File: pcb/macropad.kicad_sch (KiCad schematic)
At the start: 23 parts, among them SW1 SW_Push, SW2 SW_Push, SW3 SW_Push, SW4 SW_Push, SW5 SW_Push, SW6 SW_Push, SW7 SW_Push, SW8 SW_Push, SW9 SW_Push, U1 PICO_RP2040

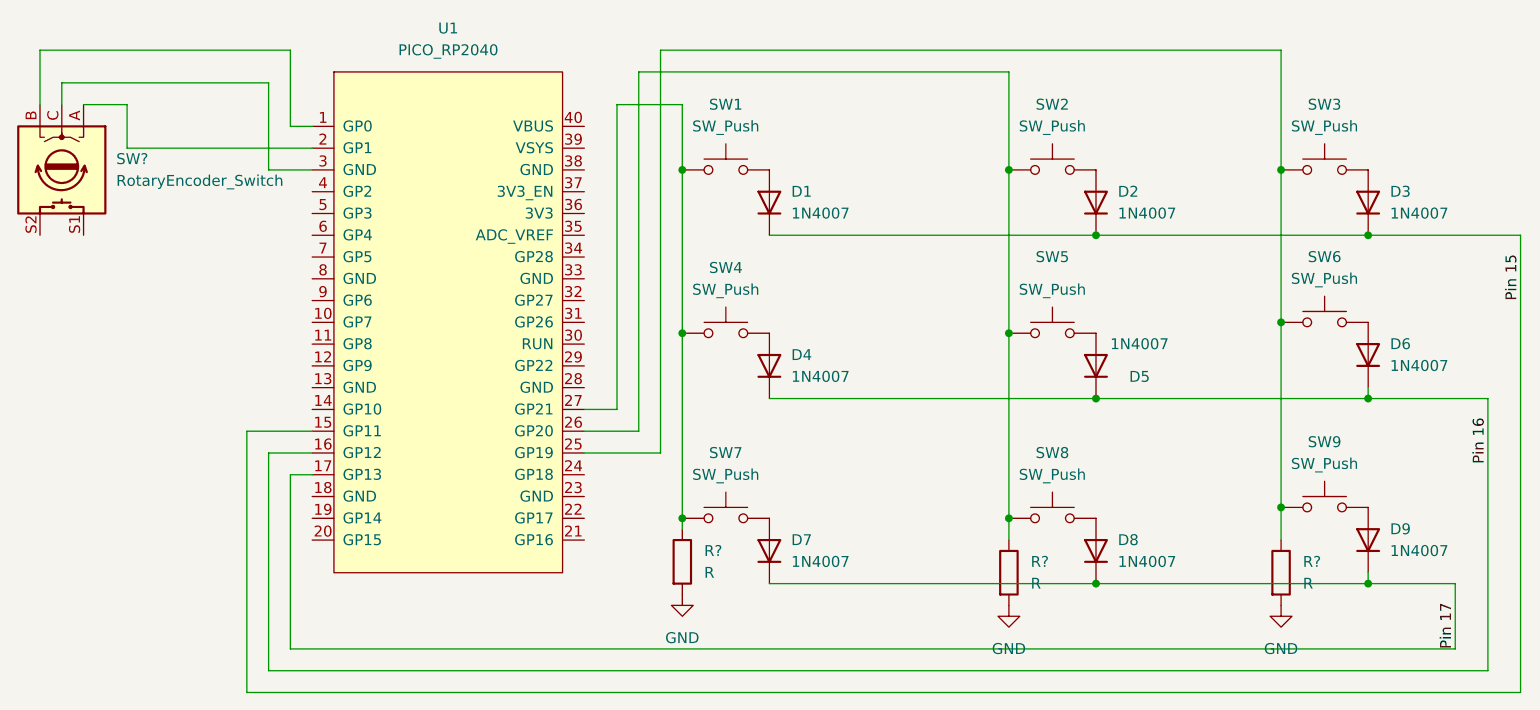
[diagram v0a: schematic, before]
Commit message: Corrected footprints for resistors
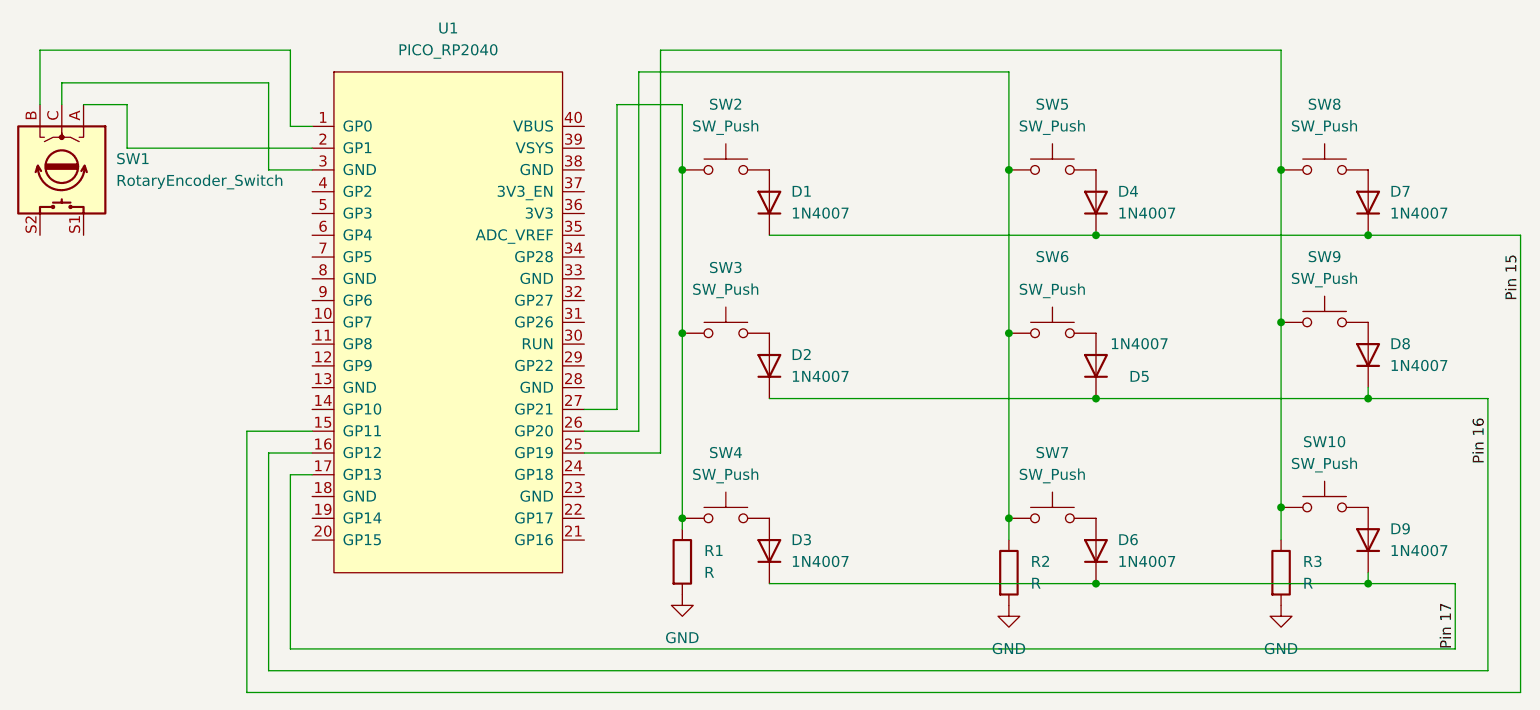
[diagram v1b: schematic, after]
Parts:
- R1, R2, R3: renamed from R?; footprint (none) -> Resistor_THT:R_Axial_DIN0207_L6.3mm_D2.5mm_P7.62mm_Horizontal
- SW1: renamed from SW?; footprint (none) -> Rotary_Encoder:RotaryEncoder_Alps_EC11E-Switch_Vertical_H20mm
- SW10: renamed from SW9; footprint (none) -> Button_Switch_THT:KSA_Tactile_SPST
- SW2: renamed from SW1; footprint (none) -> Button_Switch_THT:KSA_Tactile_SPST
- SW3: renamed from SW4; footprint (none) -> Button_Switch_THT:KSA_Tactile_SPST
- SW4: renamed from SW7; footprint (none) -> Button_Switch_THT:KSA_Tactile_SPST
- SW5: renamed from SW2; footprint (none) -> Button_Switch_THT:KSA_Tactile_SPST
- SW6: renamed from SW5; footprint (none) -> Button_Switch_THT:KSA_Tactile_SPST
- SW7: renamed from SW8; footprint (none) -> Button_Switch_THT:KSA_Tactile_SPST
- SW8: renamed from SW3; footprint (none) -> Button_Switch_THT:KSA_Tactile_SPST
- SW9: renamed from SW6; footprint (none) -> Button_Switch_THT:KSA_Tactile_SPST
- U1: footprint (none) -> MacropadFootprints:RPiPico
- renumbered D4 to D2, D7 to D3, D2 to D4, D8 to D6, D3 to D7, D6 to D8

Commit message: Finished pcb layout
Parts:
- SW10, SW2, SW3, SW4, SW5, SW6, SW7, SW8, SW9: footprint Button_Switch_THT:KSA_Tactile_SPST -> Button_Switch_Keyboard:SW_Cherry_MX_1.00u_PCB
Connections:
- net at SW1.A: now also U1.9 (GP6); no longer U1.2 (GP1)
- net at SW1.B: now also U1.7 (GP5); no longer U1.1 (GP0)
- net at SW1.C: now also U1.8 (GND); no longer U1.3 (GND)
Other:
- moved on the sheet: SW1

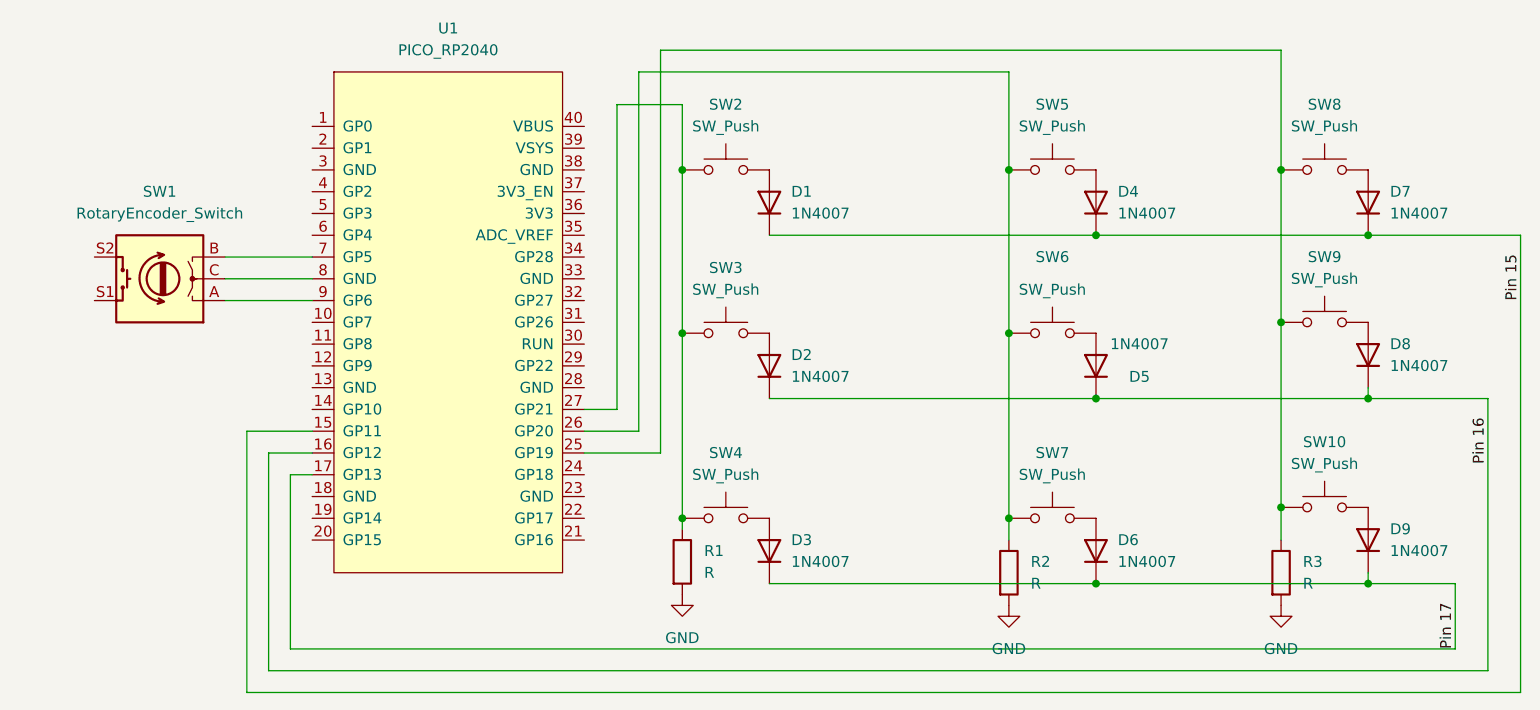
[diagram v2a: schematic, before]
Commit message: Added leds and connected switch from rotary encoder
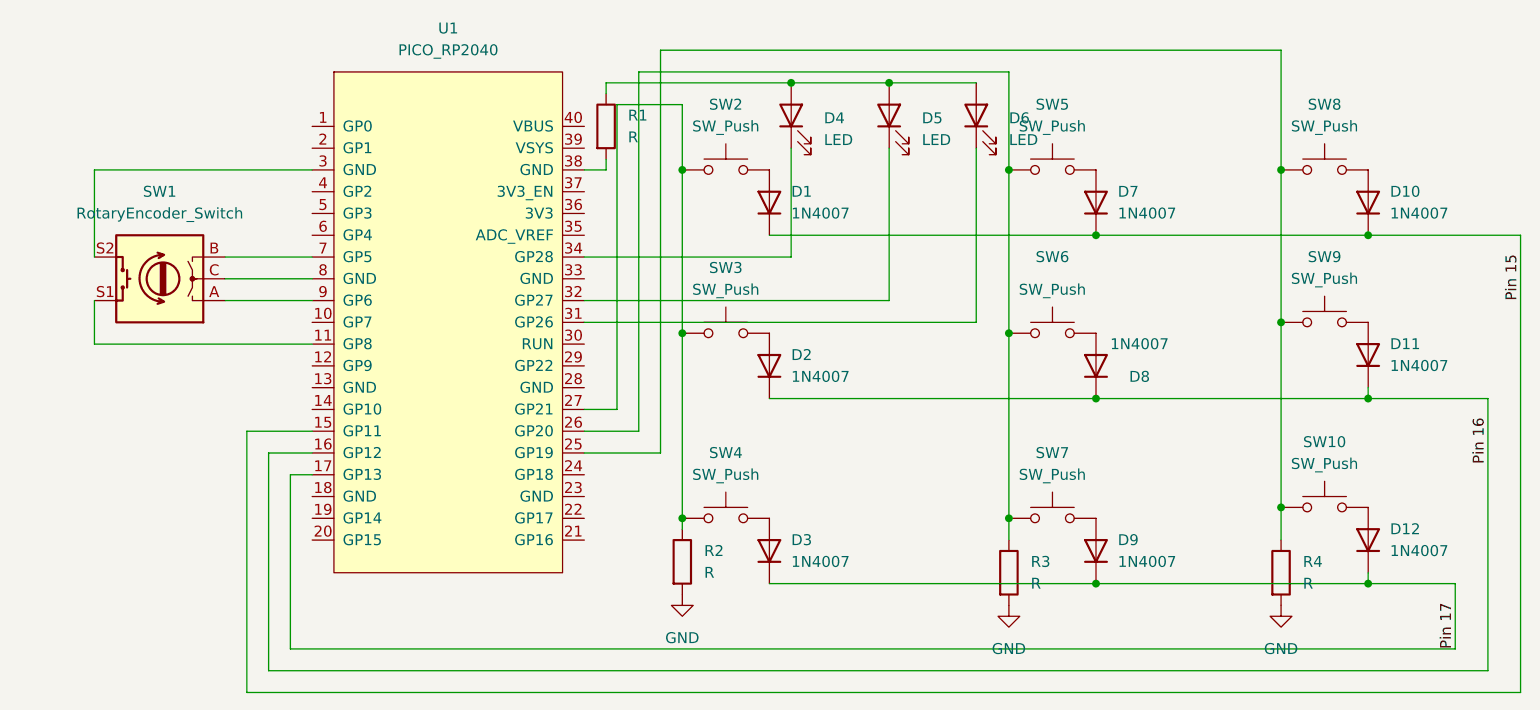
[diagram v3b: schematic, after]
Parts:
- added D4, D5, D6: LED, LED_THT:LED_D3.0mm, symbol Device:LED
- added R1: R, symbol Device:R
- renumbered D7 to D10, D8 to D11, D9 to D12, D4 to D7, D5 to D8, D6 to D9, R1 to R2, R2 to R3, R3 to R4
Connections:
- net at SW1.S1: now also U1.11 (GP8)
- net at SW1.S2: now also U1.3 (GND)
- net at U1.31 (GP26): now also D6.1 (K)
- net at U1.32 (GP27): now also D5.1 (K)
- net at U1.34 (GP28): now also D4.1 (K)
- net at U1.38 (GND): now also R1.2
- new net: D4.2 (A), D5.2 (A), D6.2 (A), R1.1
